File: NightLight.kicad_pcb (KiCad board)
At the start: 2 copper layers, 208.3 x 123.8 mm, 31 parts, among them Q1 BC817, Q2 BC817, U1 ESP32-C3-MINI-1, U2 LIS2DW12, U3 CP2102N, U4 LM1117-3.3, X1 USB_B_Micro, X2 Conn_01x04_Female

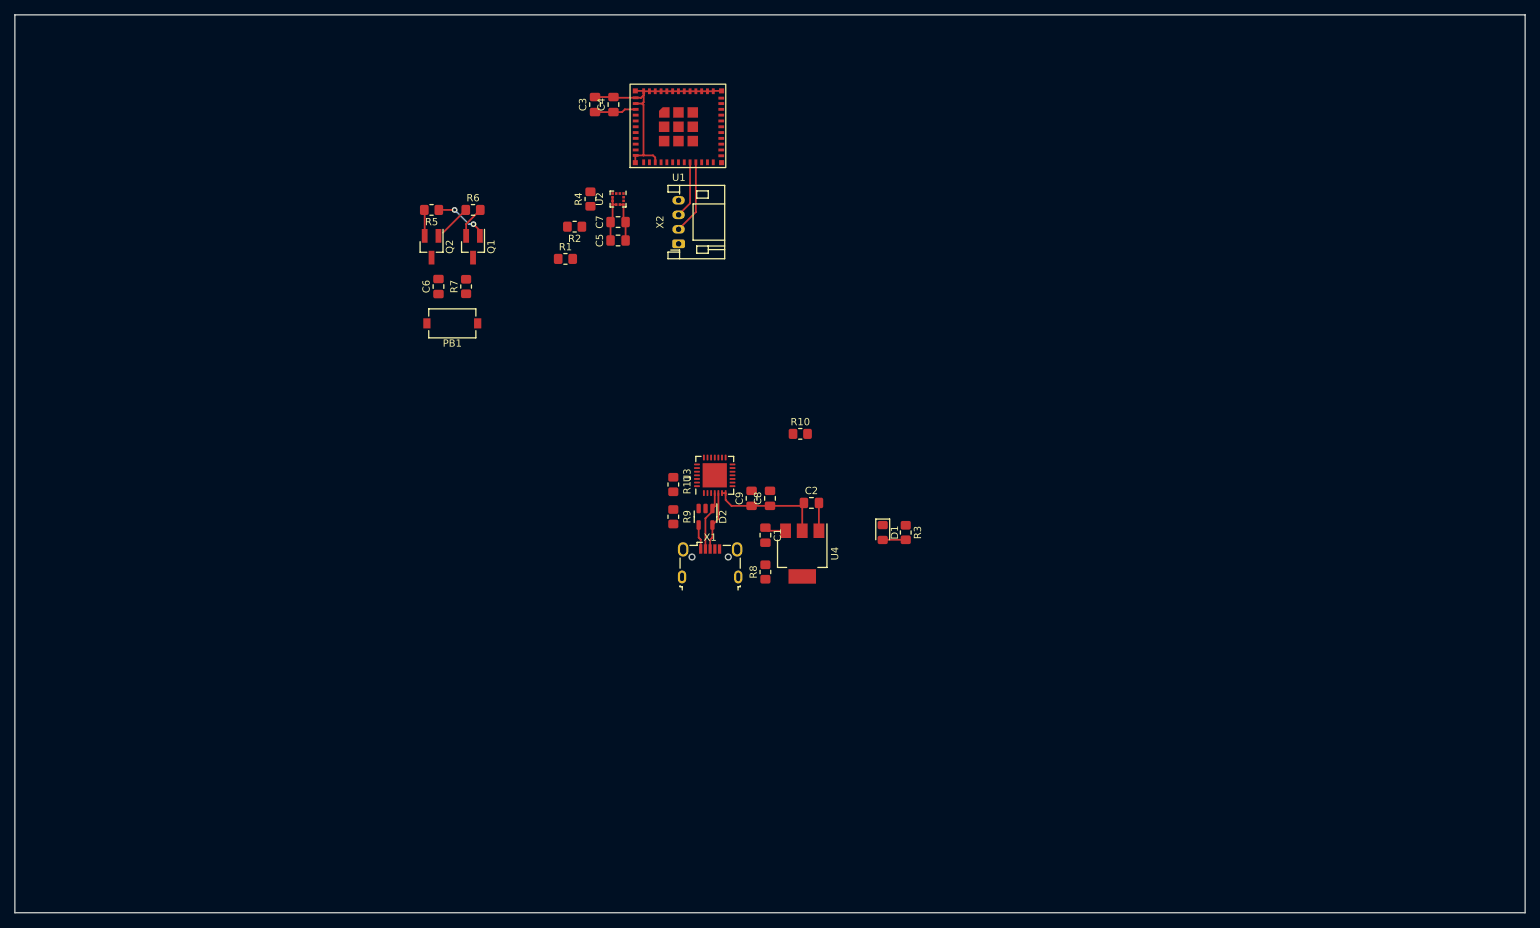
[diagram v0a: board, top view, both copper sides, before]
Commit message: Preliminary component placement on PCB.
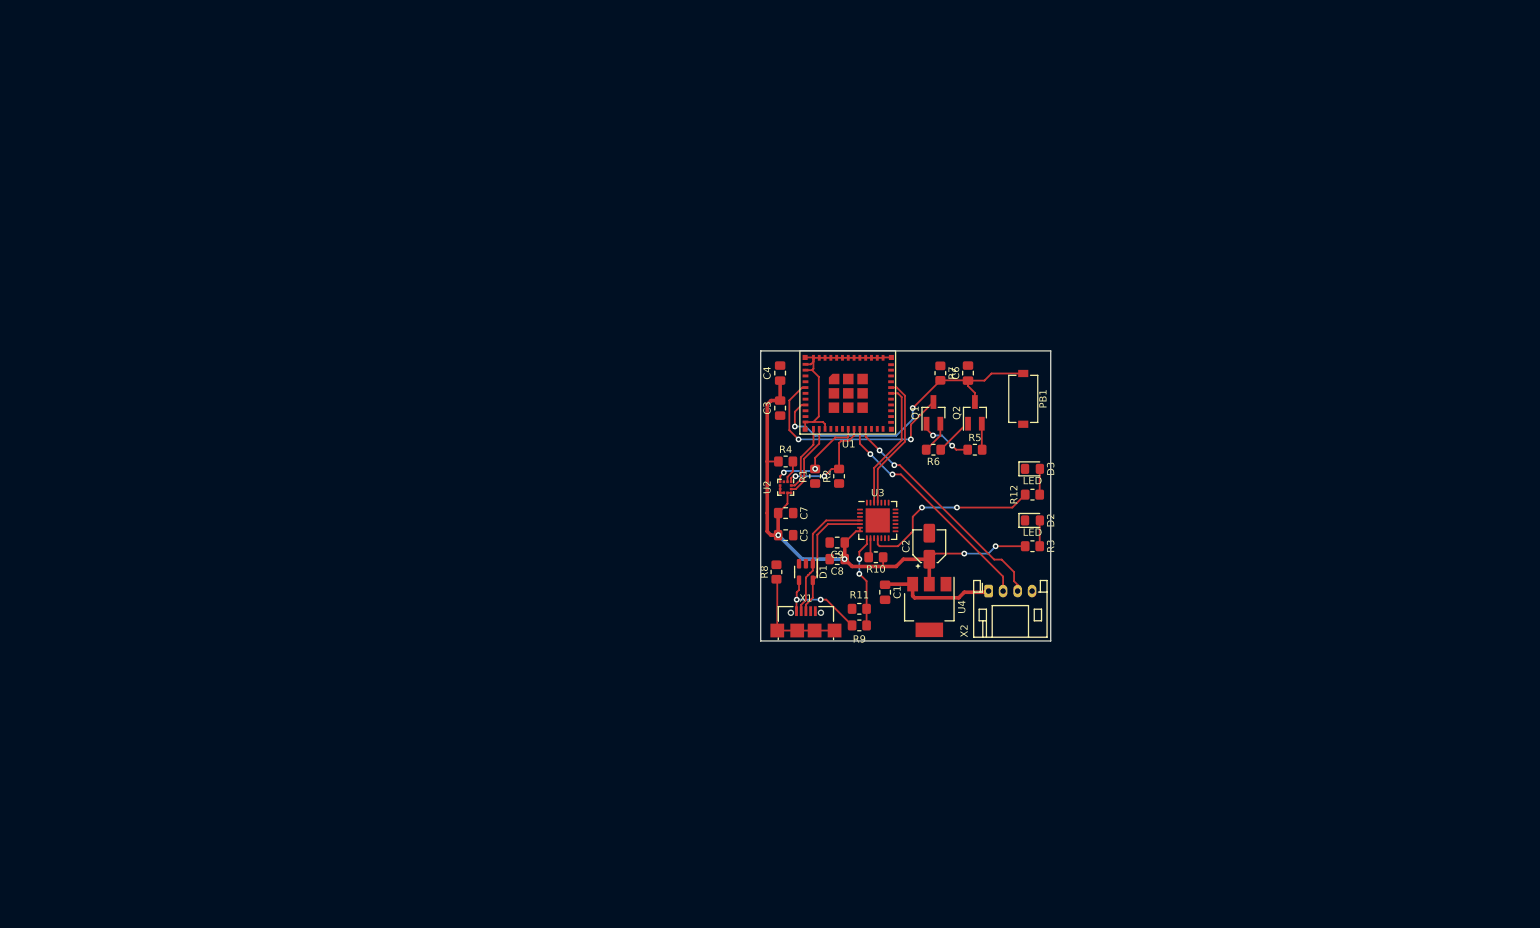
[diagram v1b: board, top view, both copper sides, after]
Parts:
- added D3: LED, Diode_SMD:D_0805_2012Metric_Pad1.15x1.40mm_HandSolder, F.Cu at (157.5, 96.3)
- added R12: 1K, Resistor_SMD:R_0805_2012Metric_Pad1.20x1.40mm_HandSolder, F.Cu at (157.5, 99.8)
- C2: value 10uF -> 22uF; footprint Capacitor_SMD:C_0805_2012Metric_Pad1.18x1.45mm_HandSolder -> Capacitor_SMD:CP_Elec_4x5.4
- X1: footprint Connector_USB:USB_Micro-B_Wuerth_629105150521 -> Custom:Wurth 629105136821
- moved R5 81.9 mm to (149.5, 93.6), turned to 0 degrees
- moved PB1 79.4 mm to (156.2, 86.6), turned to 90 degrees
- moved Q2 78.4 mm to (149.5, 88.5), turned to 90 degrees
- moved C6 74.0 mm to (148.6, 83.1)
- moved R6 71.6 mm to (143.8, 93.6), turned to 180 degrees
- moved Q1 67.5 mm to (143.8, 88.5), turned to 90 degrees
- moved R7 66.5 mm to (144.8, 83.1), turned to -90 degrees
- moved X2 64.2 mm to (151.4, 113.1), turned to 0 degrees
- moved R2 50.1 mm to (130.8, 97.3), turned to 90 degrees
- moved C3 49.0 mm to (122.7, 87.9), turned to -90 degrees
- moved C5 46.8 mm to (123.4, 105.4), turned to 0 degrees
- moved C7 46.3 mm to (123.4, 102.4), turned to 0 degrees
- moved U2 46.0 mm to (123.4, 98.8)
- moved R1 45.7 mm to (127.5, 97.3), turned to 90 degrees
- moved R4 45.1 mm to (123.4, 95.2), turned to 0 degrees
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- renumbered D2 to D1, D1 to D2
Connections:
- U1 pad 11: GND -> unconnected-(U1-Pad11)
- U1 pad 14: GND -> unconnected-(U1-Pad14)
- U1 pad 2: GND -> unconnected-(U1-Pad2)
- U1 pad 36: GND -> unconnected-(U1-Pad36)
- U1 pad 37: GND -> unconnected-(U1-Pad37)
- U1 pad 38: GND -> unconnected-(U1-Pad38)
- U1 pad 39: GND -> unconnected-(U1-Pad39)
- U1 pad 40: GND -> unconnected-(U1-Pad40)
- U1 pad 41: GND -> unconnected-(U1-Pad41)
- U1 pad 42: GND -> unconnected-(U1-Pad42)
- U1 pad 43: GND -> unconnected-(U1-Pad43)
- U1 pad 44: GND -> unconnected-(U1-Pad44)
- U1 pad 45: GND -> unconnected-(U1-Pad45)
- U1 pad 46: GND -> unconnected-(U1-Pad46)
- U1 pad 49: GND -> unconnected-(U1-Pad49)
- U1 pad 50: GND -> unconnected-(U1-Pad50)
- U1 pad 51: GND -> unconnected-(U1-Pad51)
- U1 pad 52: GND -> unconnected-(U1-Pad52)
- U1 pad 53: GND -> unconnected-(U1-Pad53)
- U3 pad 11: unconnected-(U3-Pad11) -> Net-(R12-Pad1)
- X2 pad 2: /LEDD -> /LEDC
- X2 pad 3: /LEDC -> /LEDD
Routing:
- net +3V3: track 28.1 -> 79.7 mm, vias 0 -> 4
- net /RESET: track 0.00 -> 43.7 mm, vias 0 -> 2
- net /GPIO2: track 0.00 -> 30.8 mm, vias 0 -> 2
- net Net-(R12-Pad1): track 0.00 -> 25.4 mm, vias 0 -> 2
- net /LEDC: track 7.90 -> 31.4 mm, vias 0 -> 2
- net /LEDD: track 10.2 -> 32.1 mm, vias 0 -> 2
- net /TXD0: track 0.00 -> 18.7 mm
- net /RXD0: track 0.00 -> 17.8 mm
- net Net-(R8-Pad1): track 0.00 -> 15.1 mm
- net /SDC: track 0.00 -> 14.6 mm, vias 0 -> 2
- net /SDA: track 0.00 -> 14.4 mm, vias 0 -> 2
- net GND: track 43.9 -> 29.9 mm
- net VBUS: track 2.96 -> 16.4 mm
- net Net-(R11-Pad1): track 0.00 -> 12.9 mm, vias 0 -> 2
- net Net-(D1-Pad1): track 8.25 -> 18.6 mm
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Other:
- board size 208.3 x 123.8 mm -> 40 x 40 mm

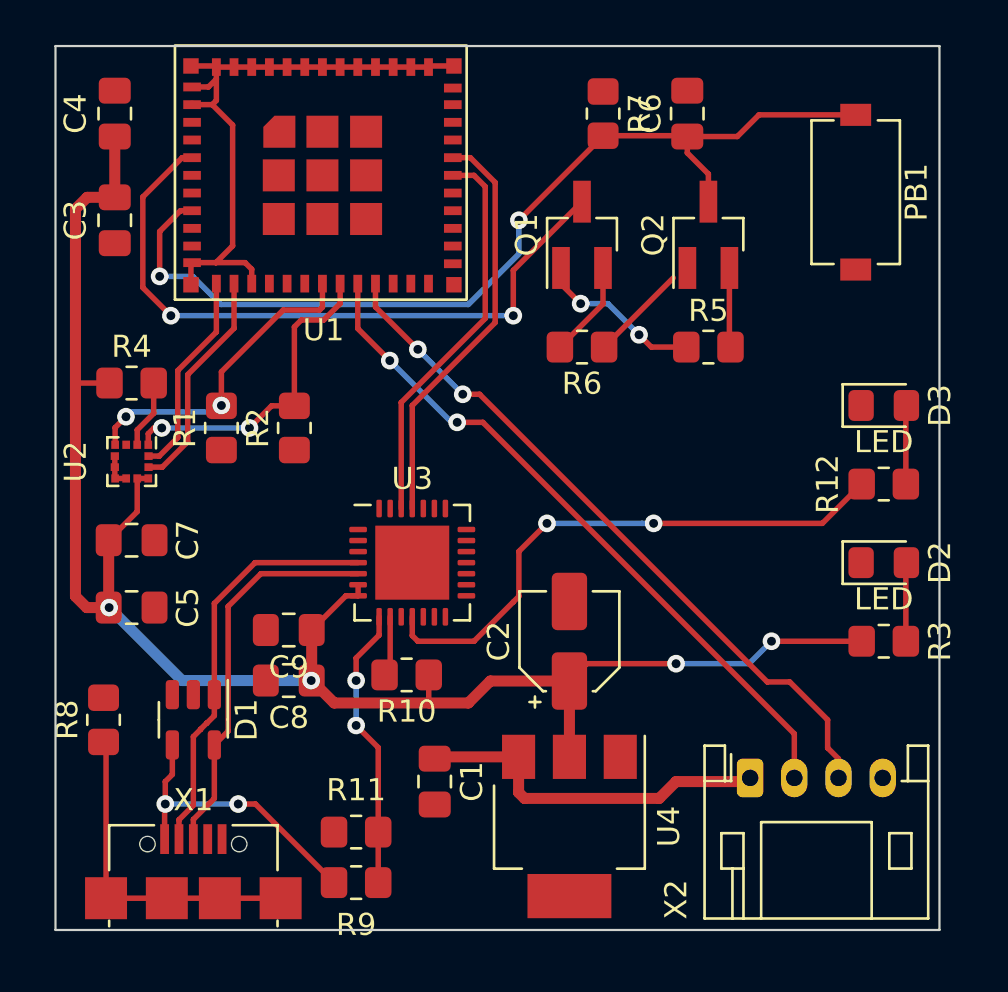
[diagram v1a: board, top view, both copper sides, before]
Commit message: Improved layout.
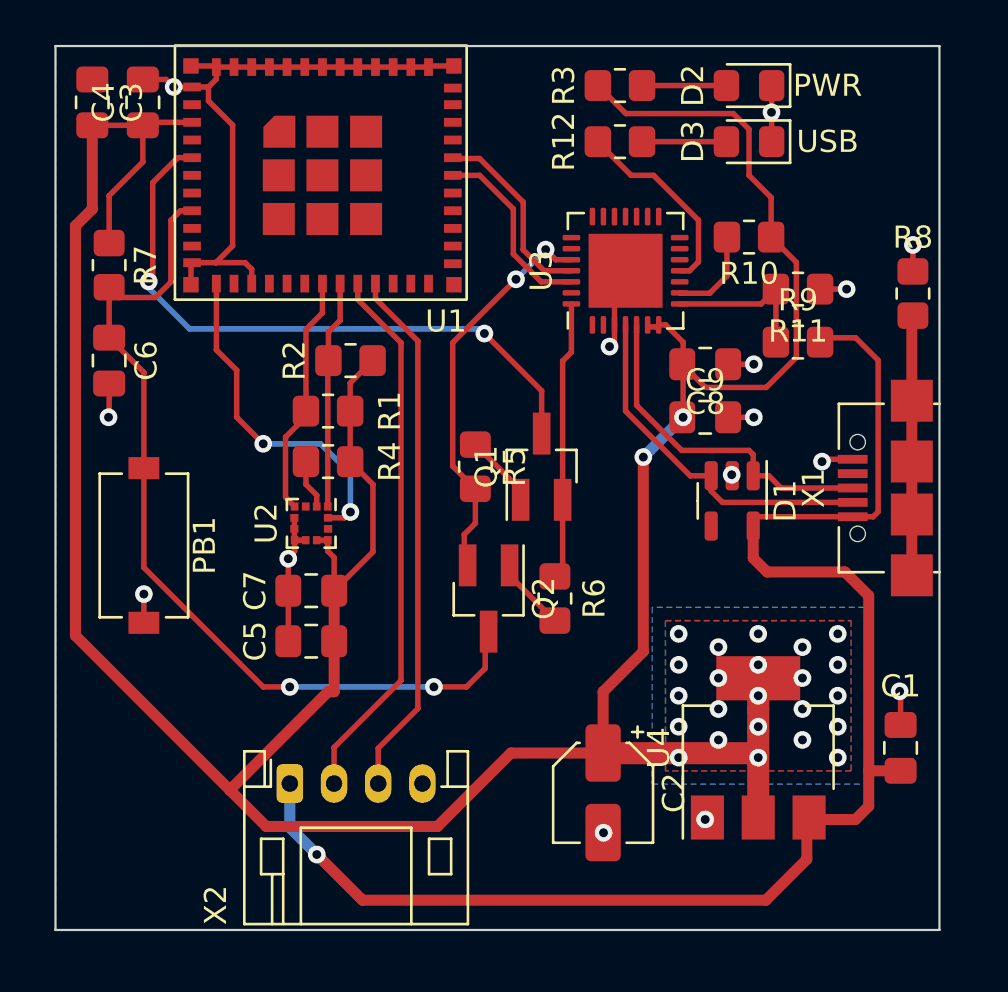
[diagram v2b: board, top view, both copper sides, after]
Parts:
- D2: value LED -> PWR
- D3: value LED -> USB
- moved R8 41.4 mm to (158.8, 91.2)
- moved X1 37.4 mm to (158.8, 100.0), turned to 90 degrees
- moved PB1 36.0 mm to (124.0, 102.6)
- moved R11 31.7 mm to (153.6, 91.0), turned to 0 degrees
- moved R9 31.6 mm to (153.6, 93.4), turned to 180 degrees
- moved C6 28.4 mm to (122.4, 94.2), turned to -90 degrees
- moved R3 27.8 mm to (145.5, 81.8)
- moved D1 26.3 mm to (150.6, 100.6)
- moved R10 25.2 mm to (151.4, 88.6)
- moved C8 23.7 mm to (149.4, 94.4), turned to 0 degrees
- moved R7 23.4 mm to (122.4, 89.9)
- moved D2 22.4 mm to (151.4, 81.8), turned to 180 degrees
- moved C9 21.2 mm to (149.4, 96.8), turned to 0 degrees
- moved C1 21.1 mm to (158.2, 111.8), turned to 90 degrees
- moved X2 20.8 mm to (130.6, 113.4)
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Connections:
- D1 pad 1: Net-(D1-Pad1) -> Net-(U3-Pad5)
- D1 pad 3: unconnected-(D1-Pad3) -> Net-(U3-Pad4)
- D1 pad 4: Net-(D1-Pad4) -> unconnected-(D1-Pad4)
- D1 pad 5: Net-(D1-Pad5) -> VBUS
- R9 pad 1: Net-(D1-Pad4) -> VBUS
- U3 pad 4: Net-(D1-Pad1) -> Net-(U3-Pad4)
- U3 pad 5: Net-(D1-Pad5) -> Net-(U3-Pad5)
- X1 pad 1: Net-(D1-Pad4) -> VBUS
- X1 pad 2: Net-(D1-Pad1) -> Net-(U3-Pad4)
- X1 pad 3: Net-(D1-Pad5) -> Net-(U3-Pad5)
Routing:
- net +3V3: track 79.7 -> 150.8 mm, vias 4 -> 25
- net VBUS: track 16.4 -> 66.6 mm, vias 0 -> 1
- net GND: track 29.9 -> 52.6 mm, vias 0 -> 15
- net Net-(D1-Pad1): track 18.6 -> 0.00 mm
- net Net-(D1-Pad5): track 17.7 -> 0.00 mm
- net Net-(R12-Pad1): track 25.4 -> 8.94 mm, vias 2 -> 0
- net Net-(U3-Pad4): track 0.00 -> 16.3 mm
- net Net-(U3-Pad5): track 0.00 -> 15.5 mm
- net /RTS: track 3.60 -> 18.1 mm, vias 0 -> 2
- net Net-(D1-Pad4): track 13.5 -> 0.00 mm, vias 2 -> 0
- net /INT2: track 10.3 -> 0.00 mm
- net /TXD0: track 18.7 -> 8.75 mm
- net /RXD0: track 17.8 -> 8.55 mm
- net /DTR: track 4.39 -> 12.7 mm
- net /LEDD: track 32.1 -> 24.2 mm, vias 2 -> 0
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- added copper zone on B.Cu, net +3V3
- added copper zone on F.Cu, net +3V3
- added copper zone on B.Cu, net GND

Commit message: WIP
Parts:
- moved R2 0.17 mm to (133.4, 94.4)
- moved R1 0.10 mm to (132.4, 96.6)
- moved R7 0.09 mm to (122.4, 90.0)
- moved C3 0.08 mm to (121.6, 82.6)
- moved C4 0.07 mm to (123.9, 82.6)
- moved R4 0.07 mm to (132.4, 98.8)
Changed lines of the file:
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@@
   )
   (footprint "Capacitor_SMD:C_0805_2012Metric_Pad1.18x1.45mm_HandSolder" (layer "F.Cu")
-    (at 122.428 94.234 -90)
+    (at 122.4 94.2 -90)
     (descr "Capacitor SMD 0805 (2012 Metric), square (rectangular) end terminal, IPC_7351 nominal with elongated pad for handsoldering. (Body size source: IPC-SM-782 page 76, https://www.pcb-3d.com/wordpress/wp-content/uploads/ipc-sm-782a_amendment_1_and_2.pdf, https://docs.google.com/spreadsheets/d/1BsfQQcO9C6DZCsRaXUlFlo91Tg2WpOkGARC1WS5S8t0/edit?usp=sharing), generated with kicad-footprint-generator")
     (tags "capacitor handsolder")
@@
     (property "Sheetfile" "NightLight.kicad_sch")
     (property "Sheetname" "")
+    (attr smd)
     (fp_text reference "U1" (at 5.588 6.604 unlocked) (layer "F.SilkS")
       (effects (font (size 1 1) (thickness 0.15)))
@@
   )
   (footprint "Resistor_SMD:R_0805_2012Metric_Pad1.20x1.40mm_HandSolder" (layer "F.Cu")
-    (at 133.35 94.234 180)
+    (at 133.4 94.4 180)
     (descr "Resistor SMD 0805 (2012 Metric), square (rectangular) end terminal, IPC_7351 nominal with elongated pad for handsoldering. (Body size source: IPC-SM-782 page 72, https://www.pcb-3d.com/wordpress/wp-content/uploads/ipc-sm-782a_amendment_1_and_2.pdf), generated with kicad-footprint-generator")
     (tags "resistor handsolder")
@@
   )
   (footprint "Capacitor_SMD:C_0805_2012Metric_Pad1.18x1.45mm_HandSolder" (layer "F.Cu")
-    (at 123.952 82.55 90)
+    (at 123.9 82.6 90)
     (descr "Capacitor SMD 0805 (2012 Metric), square (rectangular) end terminal, IPC_7351 nominal with elongated pad for handsoldering. (Body size source: IPC-SM-782 page 76, https://www.pcb-3d.com/wordpress/wp-content/uploads/ipc-sm-782a_amendment_1_and_2.pdf, https://docs.google.com/spreadsheets/d/1BsfQQcO9C6DZCsRaXUlFlo91Tg2WpOkGARC1WS5S8t0/edit?usp=sharing), generated with kicad-footprint-generator")
     (tags "capacitor handsolder")
@@
     (property "Sheetname" "")
     (attr smd)
-    (fp_text reference "C4" (at 0 -1.778 90) (layer "F.SilkS")
+    (fp_text reference "C4" (at -2.6 0.048 180) (layer "F.SilkS")
       (effects (font (size 1 1) (thickness 0.15)))
     )
@@
   )
   (footprint "Capacitor_SMD:C_0805_2012Metric_Pad1.18x1.45mm_HandSolder" (layer "F.Cu")
-    (at 121.666 82.55 90)
+    (at 121.6 82.6 90)
     (descr "Capacitor SMD 0805 (2012 Metric), square (rectangular) end terminal, IPC_7351 nominal with elongated pad for handsoldering. (Body size source: IPC-SM-782 page 76, https://www.pcb-3d.com/wordpress/wp-content/uploads/ipc-sm-782a_amendment_1_and_2.pdf, https://docs.google.com/spreadsheets/d/1BsfQQcO9C6DZCsRaXUlFlo91Tg2WpOkGARC1WS5S8t0/edit?usp=sharing), generated with kicad-footprint-generator")
     (tags "capacitor handsolder")
@@
     (property "Sheetname" "")
     (attr smd)
-    (fp_text reference "C3" (at 0 1.778 90) (layer "F.SilkS")
+    (fp_text reference "C3" (at -2.6 0 180) (layer "F.SilkS")
       (effects (font (size 1 1) (thickness 0.15)))
     )
@@
     (property "Sheetname" "")
     (attr smd)
-    (fp_text reference "Q2" (at 0 -2.5 90) (layer "F.SilkS")
+    (fp_text reference "Q2" (at 0 2.4 90) (layer "F.SilkS")
       (effects (font (size 1 1) (thickness 0.15)))
     )
@@
   )
   (footprint "Resistor_SMD:R_0805_2012Metric_Pad1.20x1.40mm_HandSolder" (layer "F.Cu")
-    (at 139 99.036 -90)
+    (at 139 99 -90)
     (descr "Resistor SMD 0805 (2012 Metric), square (rectangular) end terminal, IPC_7351 nominal with elongated pad for handsoldering. (Body size source: IPC-SM-782 page 72, https://www.pcb-3d.com/wordpress/wp-content/uploads/ipc-sm-782a_amendment_1_and_2.pdf), generated with kicad-footprint-generator")
     (tags "resistor handsolder")
@@
     (property "Sheetname" "")
     (attr smd)
-    (fp_text reference "R5" (at 0 -1.778 90) (layer "F.SilkS")
+    (fp_text reference "R5" (at -2.6 0 180) (layer "F.SilkS")
       (effects (font (size 1 1) (thickness 0.15)))
     )
@@
   )
   (footprint "Resistor_SMD:R_0805_2012Metric_Pad1.20x1.40mm_HandSolder" (layer "F.Cu")
-    (at 132.334 96.52 180)
+    (at 132.4 96.6 180)
     (descr "Resistor SMD 0805 (2012 Metric), square (rectangular) end terminal, IPC_7351 nominal with elongated pad for handsoldering. (Body size source: IPC-SM-782 page 72, https://www.pcb-3d.com/wordpress/wp-content/uploads/ipc-sm-782a_amendment_1_and_2.pdf), generated with kicad-footprint-generator")
     (tags "resistor handsolder")
@@
   )
   (footprint "Package_TO_SOT_SMD:SOT-23_Handsoldering" (layer "F.Cu")
-    (at 142 99.036 90)
+    (at 142 99 90)
     (descr "SOT-23, Handsoldering")
     (tags "SOT-23")
@@
     (property "Sheetname" "")
     (attr smd)
-    (fp_text reference "Q1" (at 0 -2.5 90) (layer "F.SilkS")
+    (fp_text reference "Q1" (at 0 2.6 90) (layer "F.SilkS")
       (effects (font (size 1 1) (thickness 0.15)))
     )
@@
     (property "Sheetname" "")
     (attr smd)
-    (fp_text reference "R6" (at 0 1.778 90) (layer "F.SilkS")
+    (fp_text reference "R6" (at -2.6 0 180) (layer "F.SilkS")
       (effects (font (size 1 1) (thickness 0.15)))
     )
@@
   )
   (footprint "Resistor_SMD:R_0805_2012Metric_Pad1.20x1.40mm_HandSolder" (layer "F.Cu")
-    (at 122.428 89.916 -90)
+    (at 122.4 90 -90)
     (descr "Resistor SMD 0805 (2012 Metric), square (rectangular) end terminal, IPC_7351 nominal with elongated pad for handsoldering. (Body size source: IPC-SM-782 page 72, https://www.pcb-3d.com/wordpress/wp-content/uploads/ipc-sm-782a_amendment_1_and_2.pdf), generated with kicad-footprint-generator")
     (tags "resistor handsolder")
@@
   )
   (footprint "Package_LGA:LGA-12_2x2mm_P0.5mm" (layer "F.Cu")
-    (at 131.572 101.5995 -90)
+    (at 131.6 101.6 -90)
     (descr "LGA12")
     (tags "lga land grid array")
@@
   )
   (footprint "Resistor_SMD:R_0805_2012Metric_Pad1.20x1.40mm_HandSolder" (layer "F.Cu")
-    (at 132.334 98.806 180)
+    (at 132.4 98.8 180)
     (descr "Resistor SMD 0805 (2012 Metric), square (rectangular) end terminal, IPC_7351 nominal with elongated pad for handsoldering. (Body size source: IPC-SM-782 page 72, https://www.pcb-3d.com/wordpress/wp-content/uploads/ipc-sm-782a_amendment_1_and_2.pdf), generated with kicad-footprint-generator")
     (tags "resistor handsolder")
